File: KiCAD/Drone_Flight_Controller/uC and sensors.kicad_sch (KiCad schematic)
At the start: 6 parts, among them U401 ESP32-WROOM-32, U402 DPS368, U403 BNO055

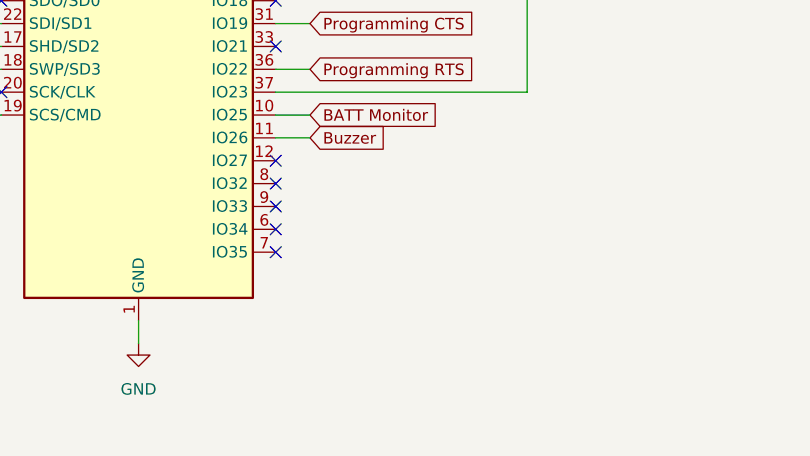
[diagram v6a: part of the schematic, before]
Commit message: Expose 3 GPIO Pins
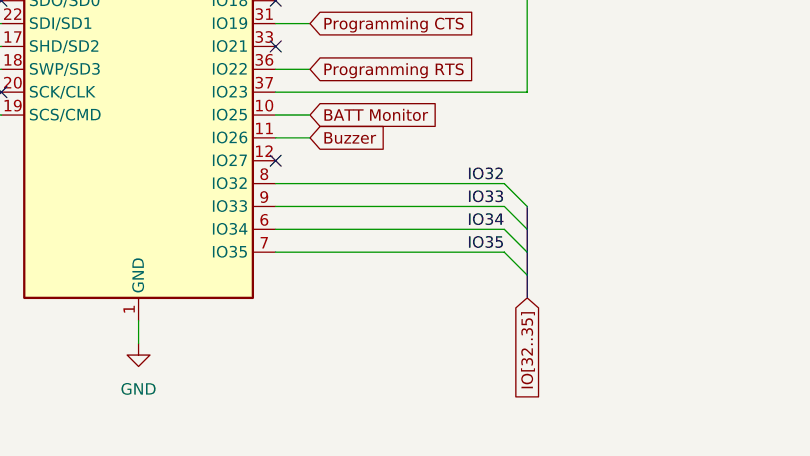
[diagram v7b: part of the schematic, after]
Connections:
- net IO34: now reaches U401.6 (IO34)
- net IO35: now reaches U401.7 (IO35)
- net IO32: now reaches U401.8 (IO32)
- net IO33: now reaches U401.9 (IO33)
- no-connect marks 15 -> 11
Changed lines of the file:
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@@
 	(title_block
 		(title "uC and sensors")
-		(date "2025-07-17")
-		(rev "V1")
+		(date "2025-09-12")
+		(rev "V2")
 		(company "HTL Steyr")
 		(comment 1 "Hinterberger")
@@
 	)
 	(no_connect
-		(at 224.79 121.92)
-	)
-	(no_connect
 		(at 194.31 93.98)
 	)
@@
 	)
 	(no_connect
-		(at 224.79 111.76)
-	)
-	(no_connect
-		(at 224.79 114.3)
-	)
-	(no_connect
-		(at 224.79 119.38)
-	)
-	(no_connect
 		(at 194.31 68.58)
 	)
@@
 	)
 	(no_connect
-		(at 224.79 116.84)
+		(at 224.79 111.76)
 	)
 	(no_connect
@@
 	(no_connect
 		(at 142.24 111.76)
+	)
+	(bus_entry
+		(at 252.73 124.46)
+		(size -2.54 -2.54)
+		(stroke
+			(width 0)
+			(type default)
+		)
 	)
 	(bus_entry
@@
 	)
 	(bus_entry
+		(at 252.73 119.38)
+		(size -2.54 -2.54)
+		(stroke
+			(width 0)
+			(type default)
+		)
+	)
+	(bus_entry
 		(at 240.03 81.28)
 		(size 2.54 -2.54)
+		(stroke
+			(width 0)
+			(type default)
+		)
+	)
+	(bus_entry
+		(at 252.73 116.84)
+		(size -2.54 -2.54)
+		(stroke
+			(width 0)
+			(type default)
+		)
+	)
+	(bus_entry
+		(at 252.73 121.92)
+		(size -2.54 -2.54)
 		(stroke
 			(width 0)
@@
 	(wire
 		(pts
+			(xy 224.79 114.3) (xy 250.19 114.3)
+		)
+		(stroke
+			(width 0)
+			(type default)
+		)
+	)
+	(wire
+		(pts
 			(xy 55.88 38.1) (xy 252.73 38.1)
 		)
@@
 		)
 	)
+	(bus
+		(pts
+			(xy 252.73 119.38) (xy 252.73 121.92)
+		)
+		(stroke
+			(width 0)
+			(type default)
+		)
+	)
 	(wire
 		(pts
@@
 	(bus
 		(pts
+			(xy 252.73 116.84) (xy 252.73 119.38)
+		)
+		(stroke
+			(width 0)
+			(type default)
+		)
+	)
+	(bus
+		(pts
 			(xy 242.57 76.2) (xy 242.57 78.74)
 		)
@@
 		)
 	)
+	(bus
+		(pts
+			(xy 252.73 124.46) (xy 252.73 127)
+		)
+		(stroke
+			(width 0)
+			(type default)
+		)
+	)
 	(wire
 		(pts
@@
 	(wire
 		(pts
+			(xy 224.79 116.84) (xy 250.19 116.84)
+		)
+		(stroke
+			(width 0)
+			(type default)
+		)
+	)
+	(wire
+		(pts
+			(xy 224.79 119.38) (xy 250.19 119.38)
+		)
+		(stroke
+			(width 0)
+			(type default)
+		)
+	)
+	(wire
+		(pts
 			(xy 194.31 96.52) (xy 189.23 96.52)
 		)
@@
 		)
 	)
+	(bus
+		(pts
+			(xy 252.73 121.92) (xy 252.73 124.46)
+		)
+		(stroke
+			(width 0)
+			(type default)
+		)
+	)
 	(wire
 		(pts
@@
 		(pts
 			(xy 209.55 53.34) (xy 209.55 55.88)
+		)
+		(stroke
+			(width 0)
+			(type default)
+		)
+	)
+	(wire
+		(pts
+			(xy 224.79 121.92) (xy 250.19 121.92)
 		)
 		(stroke
@@
 		)
 	)
+	(label "IO33"
+		(at 250.19 116.84 180)
+		(effects
+			(font
+				(size 1.27 1.27)
+			)
+			(justify right bottom)
+		)
+	)
 	(label "Motor1"
 		(at 238.76 78.74 180)
@@
 		)
 	)
+	(label "IO32"
+		(at 250.19 114.3 180)
+		(effects
+			(font
+				(size 1.27 1.27)
+			)
+			(justify right bottom)
+		)
+	)
+	(label "IO35"
+		(at 250.19 121.92 180)
+		(effects
+			(font
+				(size 1.27 1.27)
+			)
+			(justify right bottom)
+		)
+	)
+	(label "IO34"
+		(at 250.19 119.38 180)
+		(effects
+			(font
+				(size 1.27 1.27)
+			)
+			(justify right bottom)
+		)
+	)
 	(label "Motor4"
 		(at 238.76 86.36 180)
@@
 		)
 	)
+	(global_label "IO[32..35]"
+		(shape input)
+		(at 252.73 127 270)
+		(fields_autoplaced yes)
+		(effects
+			(font
+				(size 1.27 1.27)
+			)
+			(justify right)
+		)
+		(property "Intersheetrefs" "${INTERSHEET_REFS}"
+			(at 252.73 139.6615 90)
+			(effects
+				(font
+					(size 1.27 1.27)
+				)
+				(justify right)
+				(hide yes)
+			)
+		)
+	)

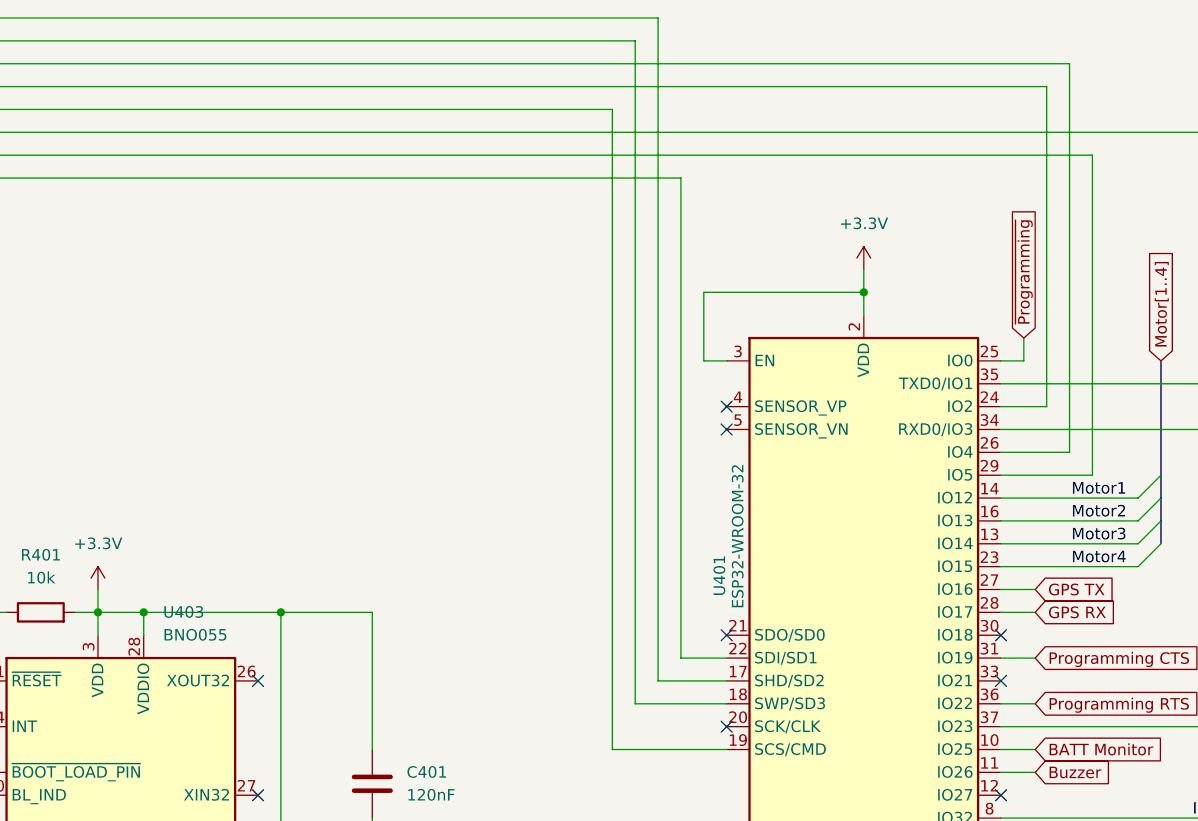
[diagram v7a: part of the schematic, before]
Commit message: Add safety resistor to programming pin
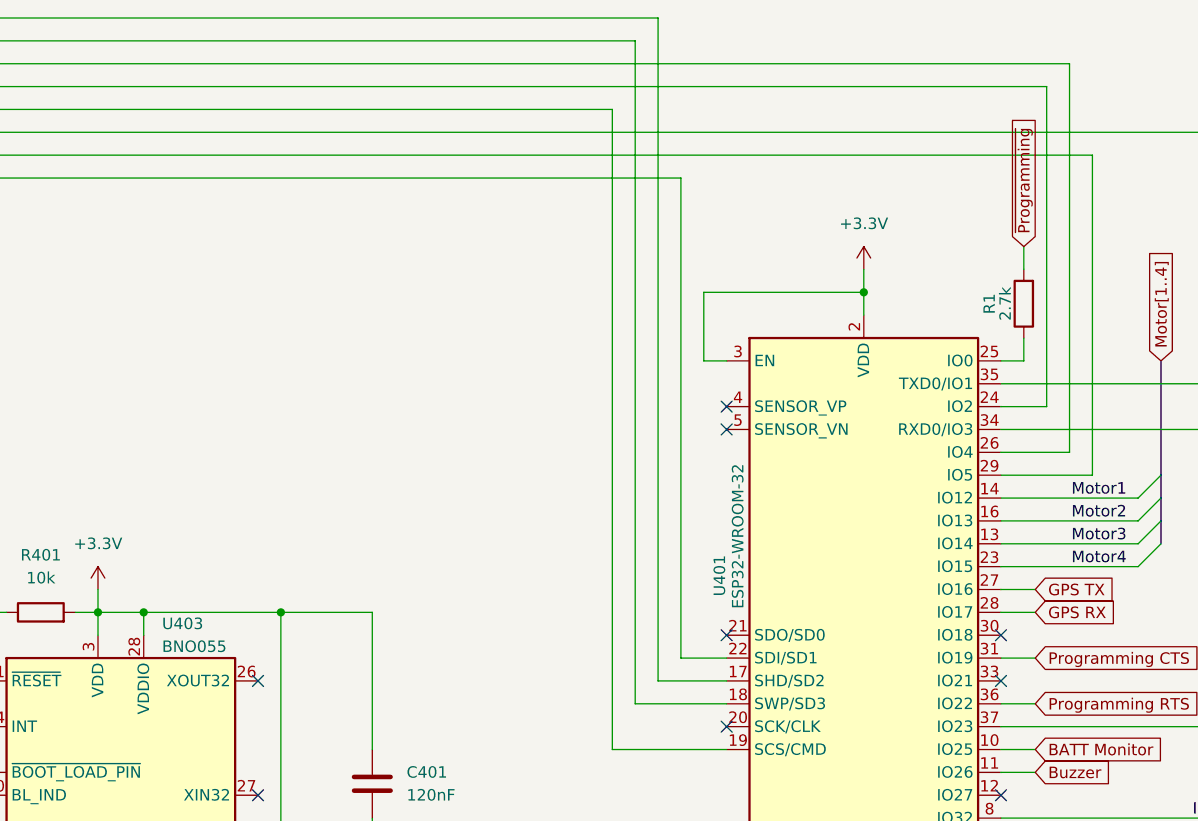
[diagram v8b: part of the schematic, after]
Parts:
- added R1: 2.7k, Resistor_SMD:R_0805_2012Metric_Pad1.20x1.40mm_HandSolder, symbol Device:R
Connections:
- net ~{Programming}: now also R1.2; no longer U401.25 (IO0)
- new net: R1.1, U401.25 (IO0)
